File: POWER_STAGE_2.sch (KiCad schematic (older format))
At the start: 13 parts, among them IC631 BTN8962TA

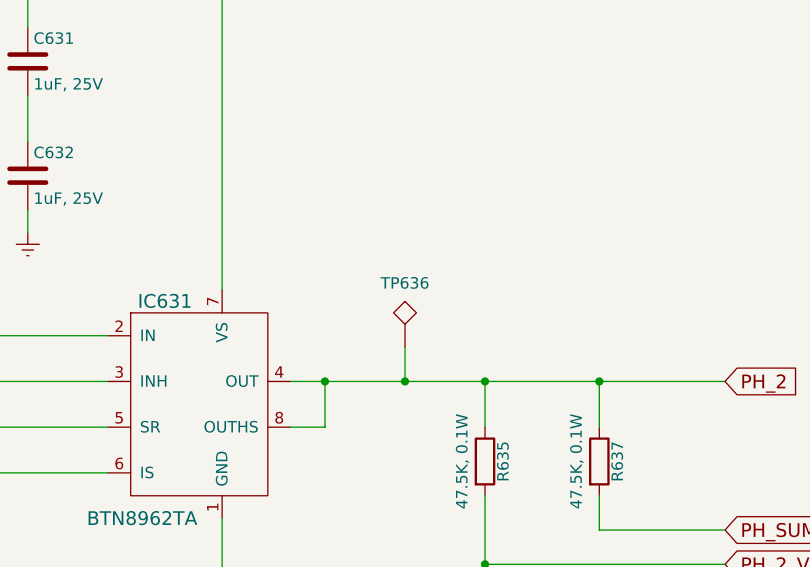
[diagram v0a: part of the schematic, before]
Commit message: - Finished traces.  Now copper areas.
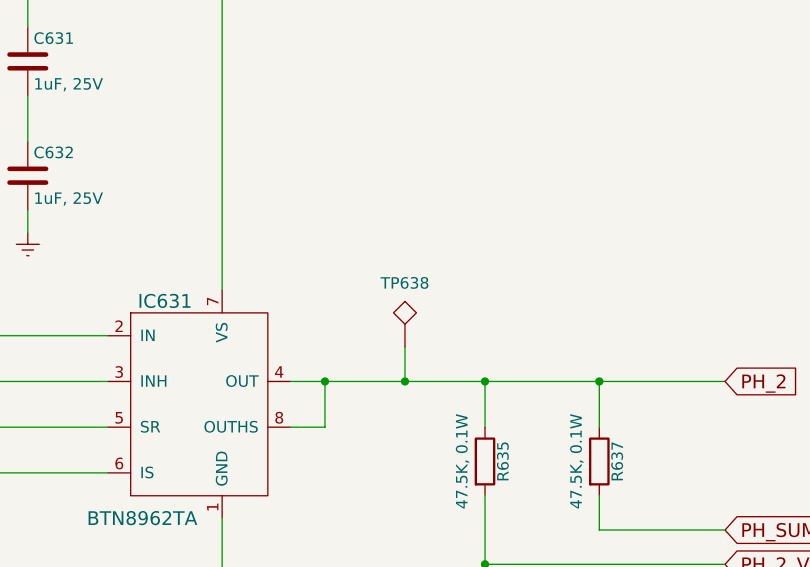
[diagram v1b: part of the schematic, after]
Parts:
- renumbered TP636 to TP638
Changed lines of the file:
@@
 	7550 5000 7550 5150
 $Comp
-L TEST TP636
+L TEST TP638
 U 1 1 5A7A40B2
 P 7200 3550
-F 0 "TP636" H 7200 3800 50  0000 C BNN
+F 0 "TP638" H 7200 3800 50  0000 C BNN
 F 1 "TEST" H 7200 3800 50  0001 C CNN
 F 2 "Measurement_Points:Measurement_Point_Round-SMD-Pad_Big" H 7200 3550 50  0001 C CNN

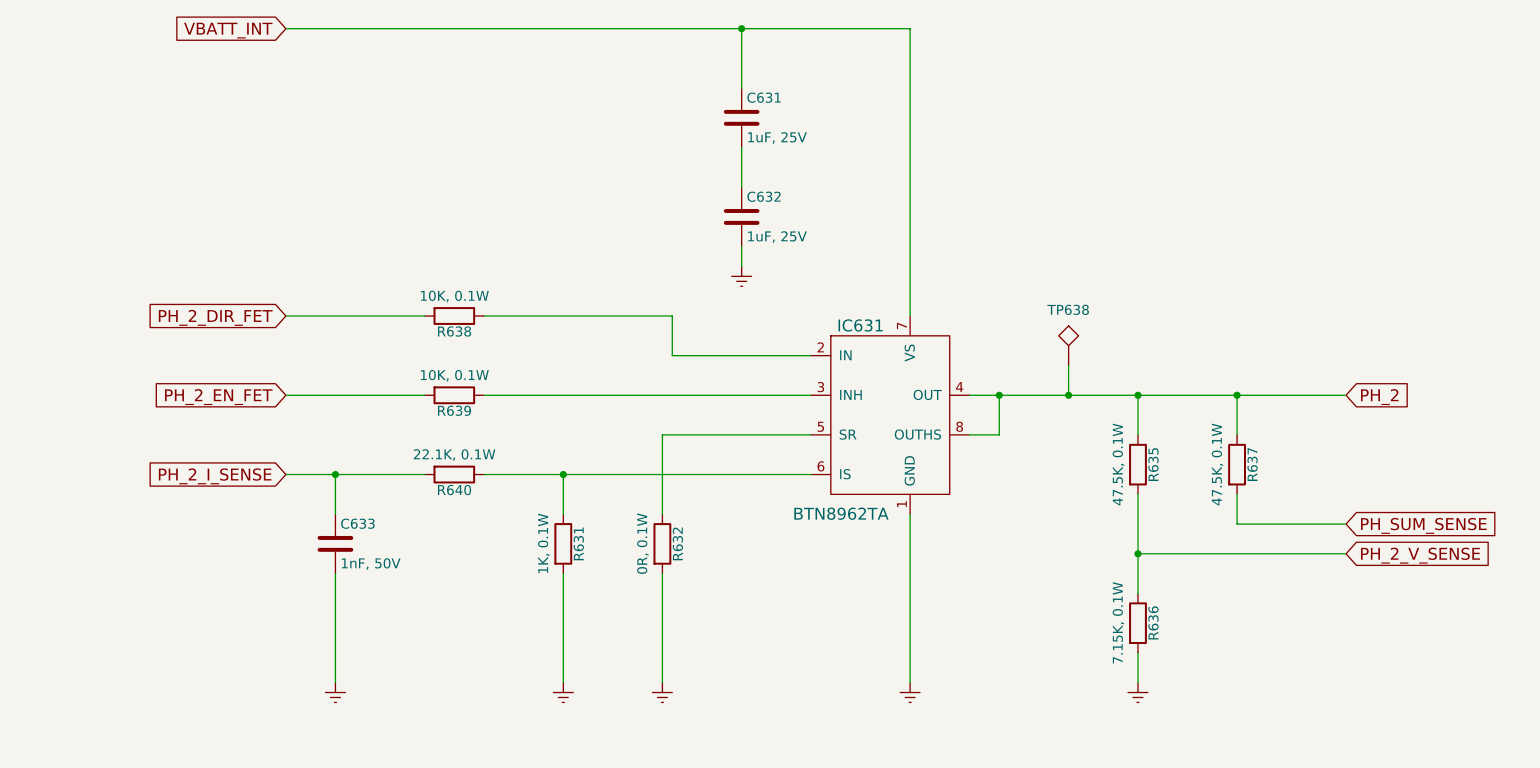
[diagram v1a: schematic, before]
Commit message: - Finished adaptation to JMS board footprint. - Added testpoints. - Changed header connector to 0.1" pitch, and tall.
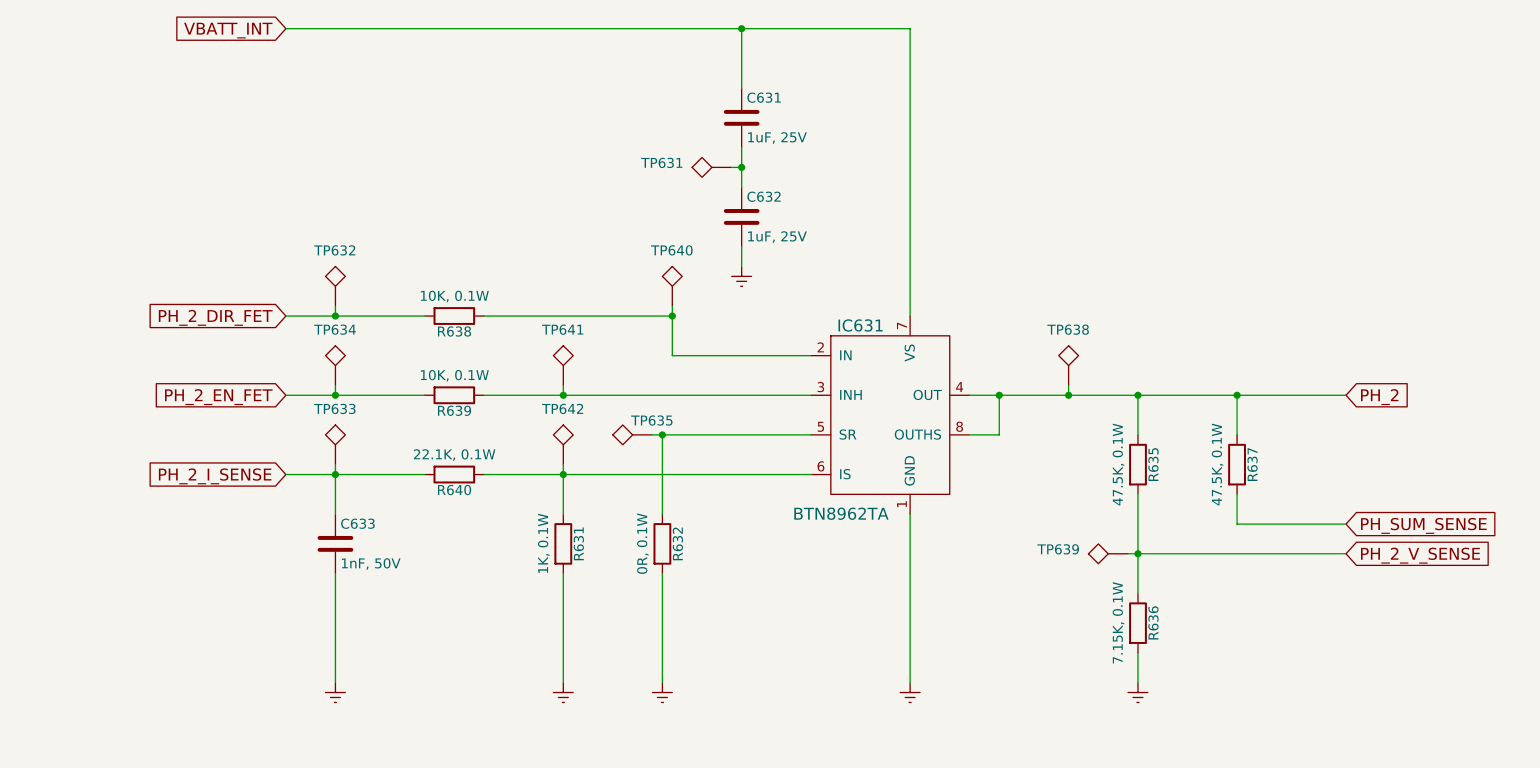
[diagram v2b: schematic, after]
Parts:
- added TP631, TP632, TP633, TP634, TP635, TP639, TP640, TP641, TP642: TEST, hp-bldc-pcb:TEST_POINT_40mil, symbol TEST
- TP638: footprint Measurement_Points:Measurement_Point_Round-SMD-Pad_Big -> hp-bldc-pcb:TEST_POINT_40mil
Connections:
- net PH_2_DIR_FET: now also TP632.1
- net PH_2_EN_FET: now also TP634.1
- net PH_2_I_SENSE: now also TP633.1
- net PH_2_V_SENSE: now also TP639.1
- net at IC631.2 (IN), R638.1: now also TP640.1
- net at IC631.3 (INH), R639.1: now also TP641.1
- net at IC631.5 (SR), R632.1: now also TP635.1
- net at IC631.6 (IS), R631.1, R640.1: now also TP642.1
- net at C631.2, C632.1: now also TP631.1
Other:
- moved on the sheet: TP638
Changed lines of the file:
@@
 	4250 3300 5200 3300
 Wire Wire Line
-	5200 3300 5200 3500
+	5200 3250 5200 3500
 Wire Wire Line
 	5200 3500 5900 3500
@@
 $EndComp
 Wire Wire Line
-	3500 4300 3500 4100
+	3500 4050 3500 4300
 Connection ~ 3500 4100
 $Comp
-L Earth #PWR043
+L Earth #PWR044
 U 1 1 5A7A403D
 P 3500 5150
-F 0 "#PWR043" H 3500 4900 50  0001 C CNN
+F 0 "#PWR044" H 3500 4900 50  0001 C CNN
 F 1 "Earth" H 3500 5000 50  0001 C CNN
 F 2 "" H 3500 5150 50  0001 C CNN
@@
 $EndComp
 Wire Wire Line
-	4650 4300 4650 4100
+	4650 4050 4650 4300
 Connection ~ 4650 4100
 Wire Wire Line
 	5150 4300 5150 3900
 Wire Wire Line
-	5150 3900 5900 3900
-$Comp
-L Earth #PWR044
+	5100 3900 5900 3900
+$Comp
+L Earth #PWR045
 U 1 1 5A7A4056
 P 4650 5150
-F 0 "#PWR044" H 4650 4900 50  0001 C CNN
+F 0 "#PWR045" H 4650 4900 50  0001 C CNN
 F 1 "Earth" H 4650 5000 50  0001 C CNN
 F 2 "" H 4650 5150 50  0001 C CNN
@@
 	4650 4600 4650 5150
 $Comp
-L Earth #PWR045
+L Earth #PWR046
 U 1 1 5A7A405D
 P 5150 5150
-F 0 "#PWR045" H 5150 4900 50  0001 C CNN
+F 0 "#PWR046" H 5150 4900 50  0001 C CNN
 F 1 "Earth" H 5150 5000 50  0001 C CNN
 F 2 "" H 5150 5150 50  0001 C CNN
@@
 	5150 4600 5150 5150
 $Comp
-L Earth #PWR046
+L Earth #PWR047
 U 1 1 5A7A4064
 P 6400 5150
-F 0 "#PWR046" H 6400 4900 50  0001 C CNN
+F 0 "#PWR047" H 6400 4900 50  0001 C CNN
 F 1 "Earth" H 6400 5000 50  0001 C CNN
 F 2 "" H 6400 5150 50  0001 C CNN
@@
 $EndComp
 $Comp
-L Earth #PWR047
+L Earth #PWR048
 U 1 1 5A7A4079
 P 5550 3050
-F 0 "#PWR047" H 5550 2800 50  0001 C CNN
+F 0 "#PWR048" H 5550 2800 50  0001 C CNN
 F 1 "Earth" H 5550 2900 50  0001 C CNN
 F 2 "" H 5550 3050 50  0001 C CNN
@@
 PH_2_V_SENSE
 Wire Wire Line
-	8600 4500 7550 4500
+	7500 4500 8600 4500
 Connection ~ 7550 4500
 $Comp
-L Earth #PWR048
+L Earth #PWR049
 U 1 1 5A7A40AB
 P 7550 5150
-F 0 "#PWR048" H 7550 4900 50  0001 C CNN
+F 0 "#PWR049" H 7550 4900 50  0001 C CNN
 F 1 "Earth" H 7550 5000 50  0001 C CNN
 F 2 "" H 7550 5150 50  0001 C CNN
@@
 L TEST TP638
 U 1 1 5A7A40B2
-P 7200 3550
-F 0 "TP638" H 7200 3800 50  0000 C BNN
-F 1 "TEST" H 7200 3800 50  0001 C CNN
-F 2 "Measurement_Points:Measurement_Point_Round-SMD-Pad_Big" H 7200 3550 50  0001 C CNN
-F 3 "" H 7200 3550 50  0001 C CNN
-	1    7200 3550
-	1    0    0    -1
-$EndComp
-Wire Wire Line
-	7200 3550 7200 3700
+P 7200 3650
+F 0 "TP638" H 7200 3900 50  0000 C BNN
+F 1 "TEST" H 7200 3900 50  0001 C CNN
+F 2 "hp-bldc-pcb:TEST_POINT_40mil" H 7200 3650 50  0001 C CNN
+F 3 "" H 7200 3650 50  0001 C CNN
+	1    7200 3650
+	1    0    0    -1
+$EndComp
+Wire Wire Line
+	7200 3650 7200 3700
 Connection ~ 7200 3700
+$Comp
+L TEST TP632
+U 1 1 5AB3BA59
+P 3500 3250
+F 0 "TP632" H 3500 3500 50  0000 C BNN
+F 1 "TEST" H 3500 3500 50  0001 C CNN
+F 2 "hp-bldc-pcb:TEST_POINT_40mil" H 3500 3250 50  0001 C CNN
+F 3 "" H 3500 3250 50  0001 C CNN
+	1    3500 3250
+	1    0    0    -1
+$EndComp
+$Comp
+L TEST TP634
+U 1 1 5AB3BAB6
+P 3500 3650
+F 0 "TP634" H 3500 3900 50  0000 C BNN
+F 1 "TEST" H 3500 3900 50  0001 C CNN
+F 2 "hp-bldc-pcb:TEST_POINT_40mil" H 3500 3650 50  0001 C CNN
+F 3 "" H 3500 3650 50  0001 C CNN
+	1    3500 3650
+	1    0    0    -1
+$EndComp
+$Comp
+L TEST TP633
+U 1 1 5AB3BAFF
+P 3500 4050
+F 0 "TP633" H 3500 4300 50  0000 C BNN
+F 1 "TEST" H 3500 4300 50  0001 C CNN
+F 2 "hp-bldc-pcb:TEST_POINT_40mil" H 3500 4050 50  0001 C CNN
+F 3 "" H 3500 4050 50  0001 C CNN
+	1    3500 4050
+	1    0    0    -1
+$EndComp
+Wire Wire Line
+	3500 3250 3500 3300
+Connection ~ 3500 3300
+Wire Wire Line
+	3500 3650 3500 3700
+Connection ~ 3500 3700
+$Comp
+L TEST TP640
+U 1 1 5AB3BC81
+P 5200 3250
+F 0 "TP640" H 5200 3500 50  0000 C BNN
+F 1 "TEST" H 5200 3500 50  0001 C CNN
+F 2 "hp-bldc-pcb:TEST_POINT_40mil" H 5200 3250 50  0001 C CNN
+F 3 "" H 5200 3250 50  0001 C CNN
+	1    5200 3250
+	1    0    0    -1
+$EndComp
+Connection ~ 5200 3300
+$Comp
+L TEST TP641
+U 1 1 5AB3BD30
+P 4650 3650
+F 0 "TP641" H 4650 3900 50  0000 C BNN
+F 1 "TEST" H 4650 3900 50  0001 C CNN
+F 2 "hp-bldc-pcb:TEST_POINT_40mil" H 4650 3650 50  0001 C CNN
+F 3 "" H 4650 3650 50  0001 C CNN
+	1    4650 3650
+	1    0    0    -1
+$EndComp
+$Comp
+L TEST TP642
+U 1 1 5AB3BD84
+P 4650 4050
+F 0 "TP642" H 4650 4300 50  0000 C BNN
+F 1 "TEST" H 4650 4300 50  0001 C CNN
+F 2 "hp-bldc-pcb:TEST_POINT_40mil" H 4650 4050 50  0001 C CNN
+F 3 "" H 4650 4050 50  0001 C CNN
+	1    4650 4050
+	1    0    0    -1
+$EndComp
+Wire Wire Line
+	4650 3650 4650 3700
+Connection ~ 4650 3700
+$Comp
+L TEST TP635
+U 1 1 5AB3BEE3
+P 5100 3900
+F 0 "TP635" V 5200 3900 50  0000 C BNN
+F 1 "TEST" H 5100 4150 50  0001 C CNN
+F 2 "hp-bldc-pcb:TEST_POINT_40mil" H 5100 3900 50  0001 C CNN
+F 3 "" H 5100 3900 50  0001 C CNN
+	1    5100 3900
+	0    -1   -1   0
+$EndComp
+Connection ~ 5150 3900
+$Comp
+L TEST TP631
+U 1 1 5AB3C5C8
+P 5500 2550
+F 0 "TP631" V 5550 2900 50  0000 C BNN
+F 1 "TEST" H 5500 2800 50  0001 C CNN
+F 2 "hp-bldc-pcb:TEST_POINT_40mil" H 5500 2550 50  0001 C CNN
+F 3 "" H 5500 2550 50  0001 C CNN
+	1    5500 2550
+	0    -1   -1   0
+$EndComp
+Wire Wire Line
+	5500 2550 5550 2550
+Connection ~ 5550 2550
+$Comp
+L TEST TP639
+U 1 1 5AB3C7CA
+P 7500 4500
+F 0 "TP639" V 7550 4850 50  0000 C BNN
+F 1 "TEST" H 7500 4750 50  0001 C CNN
+F 2 "hp-bldc-pcb:TEST_POINT_40mil" H 7500 4500 50  0001 C CNN
+F 3 "" H 7500 4500 50  0001 C CNN
+	1    7500 4500
+	0    -1   -1   0
+$EndComp
 $EndSCHEMATC

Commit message: - Minor changes to silkscreen. - Minor changes to BOM. - Additions to Readme file. - Page layout changed in schematic.
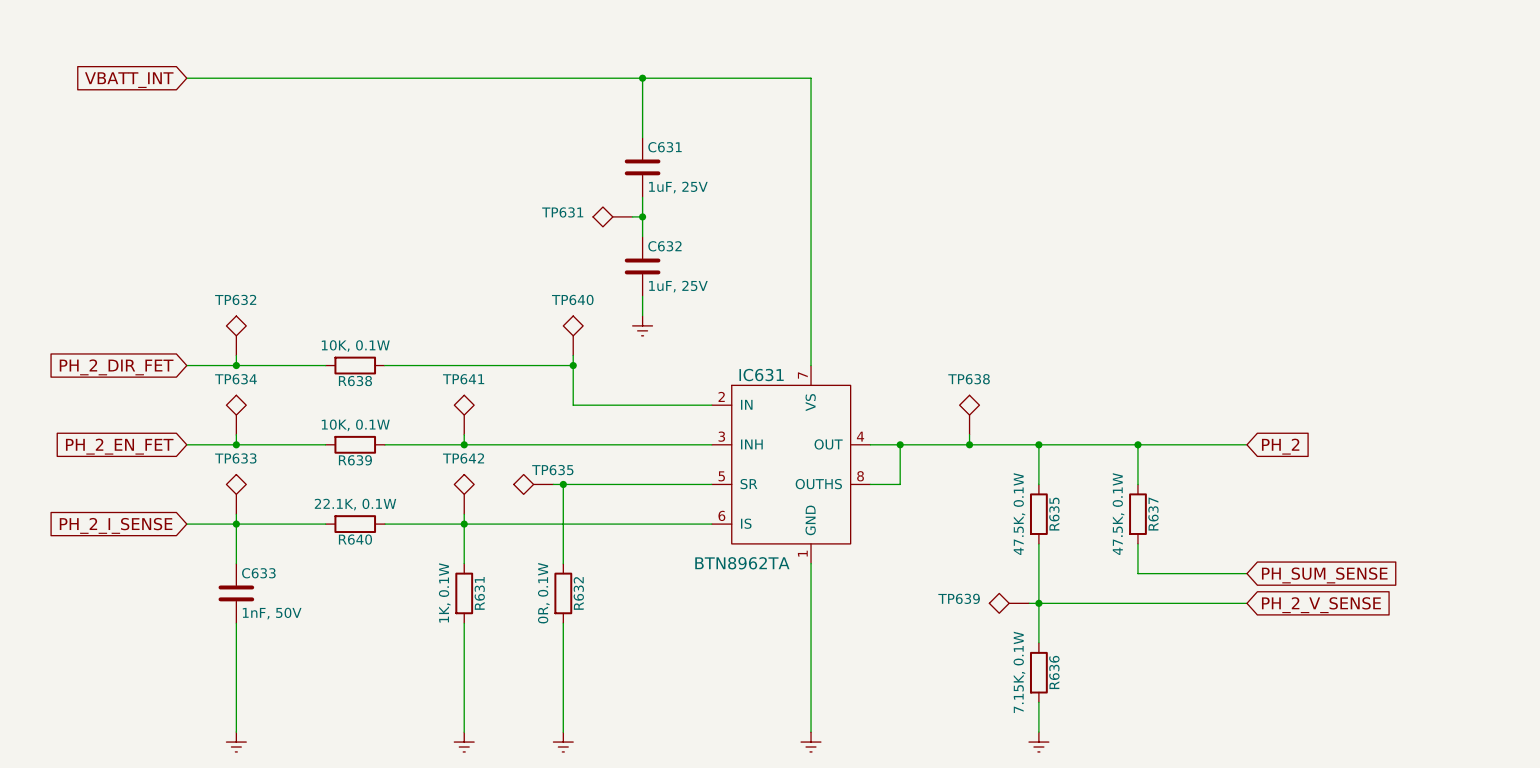
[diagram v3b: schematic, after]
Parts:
- IC631: footprint TO_SOT_Packages_SMD:TO-263-7_TabPin8 -> hp-bldc-pcb:TO-263-7_TabPin8
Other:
- moved on the sheet: C631, C632, C633, IC631, R631, R632, R635, R636, R637, R638, R639, R640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
